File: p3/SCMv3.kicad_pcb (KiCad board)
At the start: 2 copper layers, 58.7 x 110.9 mm, 121 parts, among them IC1 40106, IC2 40106, IC3 TL082, J1 ISP, J1-OUT8 JACK-MONO-SWB, J2 Conn_01x02, J2-OUT7 JACK-MONO-SWB, J3 POWER, J3-OUT6 JACK-MONO-SWB, J4-OUT5 JACK-MONO-SWB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

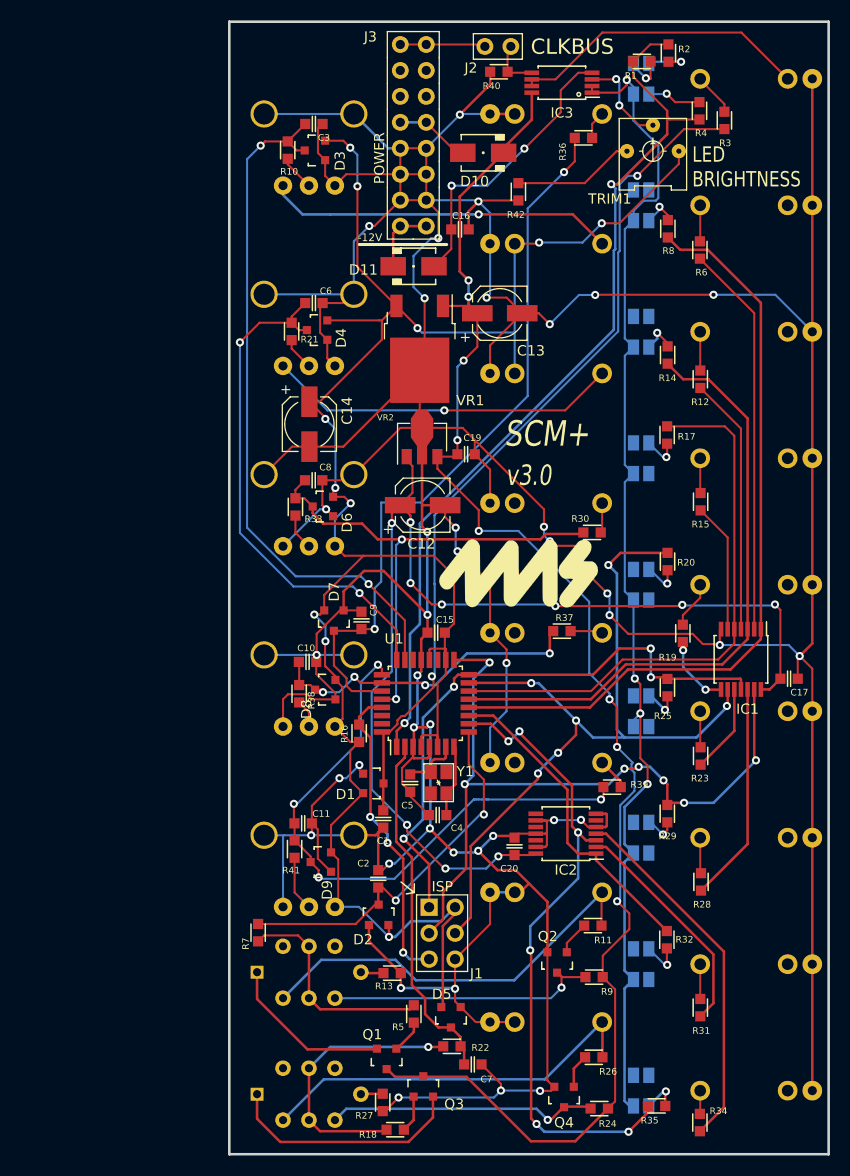
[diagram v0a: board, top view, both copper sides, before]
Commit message: p3 ready to connect pins: then route
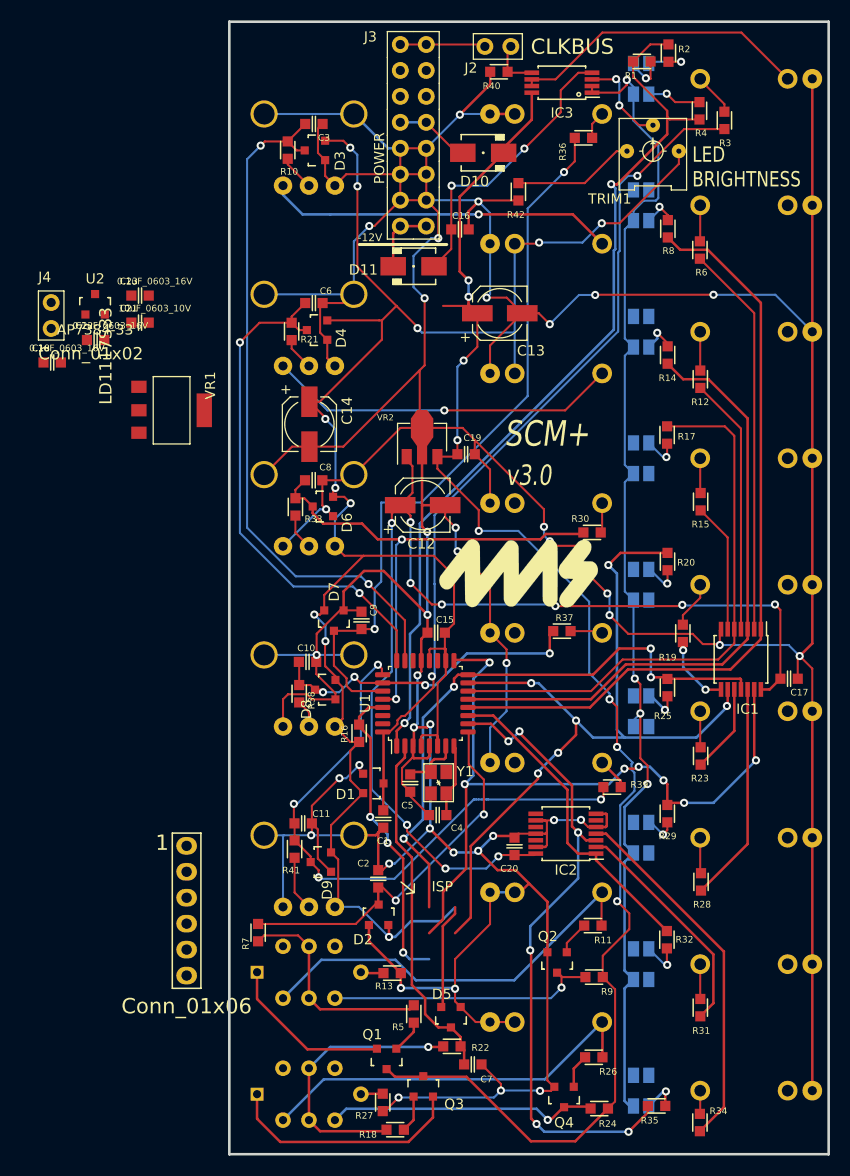
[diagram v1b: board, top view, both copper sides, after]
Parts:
- added C18: 0.1uF_0603_16V, 4ms_Capacitor:C_0603, F.Cu at (-17.3, 33.4)
- added C21: 10uF_0603_10V, 4ms_Capacitor:C_0603, F.Cu at (-8.74, 29.5)
- added C22: 0.1uF_0603_16V, 4ms_Capacitor:C_0603, F.Cu at (-13.1, 31.2)
- added C23: 0.1uF_0603_16V, 4ms_Capacitor:C_0603, F.Cu at (-8.74, 26.8)
- added J4: Conn_01x02, 4ms_Connector:Pins_1x02_2.54mm_TH, F.Cu at (-17.4, 28.8)
- added U2: AP7384-33, 4ms_Package_SOT:SOT23-3_PO132, F.Cu at (-13.1, 27.7)
- J1: value ISP -> Conn_01x06; footprint 4ms_Connector:Pins_2x03_2.54mm_TH -> 4ms_Connector:Pins_1x06_2.54mm_TH_SWD
- U1: value ATMEGA328-AU -> STM32F030K6Tx; footprint 4ms_Package_QFP:TQFP-32_7x7mm_P0.8mm -> Package_QFP:LQFP-32_7x7mm_P0.8mm
- VR1: value L78M05CDT -> LD1117S33; footprint 4ms_Package_TO:TO-252-2 -> 4ms_Package_SOT:SOT223
- moved J1 25.1 mm to (-4.18, 87.0)
- moved VR1 25.0 mm to (-5.65, 38.0)
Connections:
- net +9V renamed +8V
- net Net-(J2-Pad2) renamed /CLKBUS_PWRHDR
- C14 pad 1: +5V -> +3V3
- C15 pad 1: +5V -> -12VA
- IC1 pad 11: /UC_OUT5_MISO -> /UC_OUT5
- IC1 pad 13: /UC_OUT6_SCK -> /UC_OUT6
- IC1 pad 9: /UC_OUT4_MOSI -> /UC_OUT4
- J1 pad 1: /UC_OUT5_MISO -> +3V3
- J1 pad 2: +5V -> unconnected-(J1-Pad2)
- J1 pad 3: /UC_OUT6_SCK -> GND
- J1 pad 4: /UC_OUT4_MOSI -> /SWDIO
- J1 pad 6: GND -> unconnected-(J1-Pad6)
- R16 pad 2: +5V -> +3V3
- R20 pad 1: /UC_OUT4_MOSI -> /UC_OUT4
- R25 pad 1: /UC_OUT5_MISO -> /UC_OUT5
- R29 pad 1: /UC_OUT6_SCK -> /UC_OUT6
- TRIM1 pad 3: +5V -> +3V3
- U1 pad 1: /UC_LED_IN -> +3V3
- U1 pad 10: /UC_OUT8 -> unconnected-(U1-Pad10)
- U1 pad 11: /UC_OUT7 -> unconnected-(U1-Pad11)
- U1 pad 12: /UC_OUT1 -> unconnected-(U1-Pad12)
- U1 pad 13: /UC_OUT2 -> unconnected-(U1-Pad13)
- U1 pad 14: /UC_OUT3 -> unconnected-(U1-Pad14)
- U1 pad 15: /UC_OUT4_MOSI -> unconnected-(U1-Pad15)
- U1 pad 16: /UC_OUT5_MISO -> GND
- U1 pad 17: /UC_OUT6_SCK -> +3V3
- U1 pad 18: +5V -> unconnected-(U1-Pad18)
- U1 pad 2: /UC_MUTE -> Net-(C5-Pad1)
- U1 pad 20: +5V -> unconnected-(U1-Pad20)
- U1 pad 21: GND -> unconnected-(U1-Pad21)
- U1 pad 23: /UC_ROTATE -> /SWDIO
- U1 pad 24: /UC_SLIP -> /SWCLK
- U1 pad 25: /UC_PW -> unconnected-(U1-Pad25)
- U1 pad 26: /UC_SKIP -> unconnected-(U1-Pad26)
- U1 pad 27: /UC_SYNC -> unconnected-(U1-Pad27)
- U1 pad 28: /UC_SHUFFLE -> unconnected-(U1-Pad28)
- U1 pad 29: /RESET -> unconnected-(U1-Pad29)
- U1 pad 3: GND -> Net-(C4-Pad1)
- U1 pad 32: /UC_CLK_IN -> GND
- U1 pad 4: +5V -> /RESET
- U1 pad 5: GND -> +3.3VA
- U1 pad 6: +5V -> unconnected-(U1-Pad6)
- U1 pad 7: Net-(C5-Pad1) -> unconnected-(U1-Pad7)
- U1 pad 8: Net-(C4-Pad1) -> unconnected-(U1-Pad8)
- U1 pad 9: /UC_FAST -> unconnected-(U1-Pad9)
- VR1 pad 1: +12V -> GND
- VR1 pad 2: GND -> +3V3
- VR1 pad 3: +5V -> +12V
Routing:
- net GND: track 666.9 -> 938.0 mm, vias 40 -> 58
- net +5V: track 208.0 -> 10.3 mm, vias 11 -> 0
- net /UC_OUT4_MOSI: track 80.1 -> 0.00 mm, vias 6 -> 0
- net /UC_OUT4: track 0.00 -> 80.1 mm, vias 0 -> 6
- net /UC_OUT6_SCK: track 73.4 -> 0.00 mm, vias 7 -> 0
- net /UC_OUT5_MISO: track 58.7 -> 0.00 mm, vias 4 -> 0
- net /UC_OUT5: track 0.00 -> 58.7 mm, vias 0 -> 4
- net unconnected-(U1-Pad29): track 0.00 -> 30.3 mm, vias 0 -> 3
- net /RESET: track 30.3 -> 0.00 mm, vias 3 -> 0

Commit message: Atmega replacement and other mods
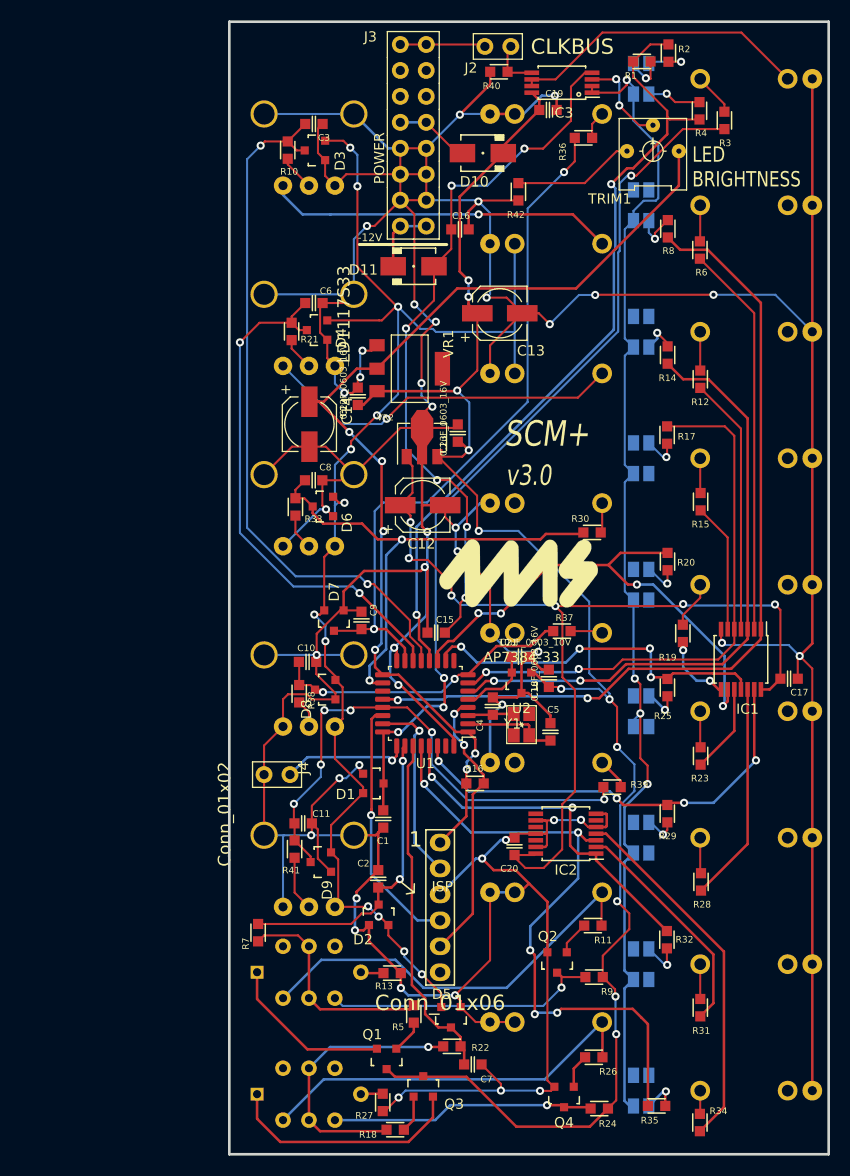
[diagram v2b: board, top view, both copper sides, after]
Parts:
- moved C18 57.6 mm to (31.3, 64.3), turned to 90 degrees
- moved U2 55.8 mm to (28.6, 64.7), turned to 180 degrees
- moved J4 50.1 mm to (4.67, 73.7), turned to -90 degrees
- moved C21 49.5 mm to (28.5, 62.2)
- moved C19 34.6 mm to (31.2, 8.64)
- moved C23 33.9 mm to (22.4, 40.3), turned to 90 degrees
- moved C22 26.3 mm to (12.6, 36.7), turned to 90 degrees
- moved J1 24.8 mm to (20.6, 86.7)
- moved VR1 23.7 mm to (17.7, 34.0)
- moved C5 14.6 mm to (31.4, 69.5), turned to 90 degrees
- moved R16 12.4 mm to (24.1, 74.6), turned to 180 degrees
- moved C4 12.0 mm to (25.8, 67.0), turned to 90 degrees
- moved Y1 9.91 mm to (28.6, 68.8), turned to -90 degrees
- turned U1 to 180 degrees
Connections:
- J1 pad 2: unconnected-(J1-Pad2) -> /SWCLK
- U1 pad 10: unconnected-(U1-Pad10) -> /UC_OUT5
- U1 pad 11: unconnected-(U1-Pad11) -> /UC_OUT4
- U1 pad 12: unconnected-(U1-Pad12) -> /UC_LED_IN
- U1 pad 13: unconnected-(U1-Pad13) -> /UC_ROTATE
- U1 pad 14: unconnected-(U1-Pad14) -> /UC_SLIP
- U1 pad 15: unconnected-(U1-Pad15) -> /UC_SYNC
- U1 pad 18: unconnected-(U1-Pad18) -> /UC_SHUFFLE
- U1 pad 20: unconnected-(U1-Pad20) -> /UC_OUT1
- U1 pad 21: unconnected-(U1-Pad21) -> /UC_PW
- U1 pad 22: unconnected-(U1-Pad22) -> /SWDIO
- U1 pad 23: /SWDIO -> /SWCLK
- U1 pad 24: /SWCLK -> /UC_CLK_IN
- U1 pad 25: unconnected-(U1-Pad25) -> /FREERUN_JMP
- U1 pad 26: unconnected-(U1-Pad26) -> /UC_FAST
- U1 pad 27: unconnected-(U1-Pad27) -> /UC_MUTE
- U1 pad 28: unconnected-(U1-Pad28) -> /UC_OUT8
- U1 pad 29: unconnected-(U1-Pad29) -> /UC_OUT7
- U1 pad 30: unconnected-(U1-Pad30) -> /UC_OUT6
- U1 pad 6: unconnected-(U1-Pad6) -> /UC_OUT2
- U1 pad 7: unconnected-(U1-Pad7) -> /UC_OUT3
- U1 pad 8: unconnected-(U1-Pad8) -> /UC_SKIP
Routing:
- net GND: track 938.0 -> 646.4 mm, vias 58 -> 41
- net +5V: track 10.3 -> 138.2 mm, vias 0 -> 12
- net +3V3: track 0.00 -> 102.7 mm, vias 0 -> 6
- net /UC_OUT6: track 0.00 -> 43.2 mm, vias 0 -> 4
- net -12VA: track 28.2 -> 70.0 mm, vias 2 -> 6
- net /UC_OUT4: track 80.1 -> 49.4 mm, vias 6 -> 4
- net unconnected-(U1-Pad29): track 30.3 -> 0.00 mm, vias 3 -> 0
- net /RESET: track 0.00 -> 27.3 mm, vias 0 -> 2
- net /SWDIO: track 0.00 -> 25.1 mm, vias 0 -> 1
- net /UC_OUT5: track 58.7 -> 35.5 mm
- net +12V: track 148.7 -> 168.0 mm, vias 8 -> 11
- net /SWCLK: track 0.00 -> 18.6 mm, vias 0 -> 1
- net +8V: track 109.3 -> 93.0 mm, vias 10 -> 6
- net /FREERUN_JMP: track 0.00 -> 12.4 mm, vias 0 -> 1
- net /UC_LED_IN: track 87.5 -> 78.8 mm
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
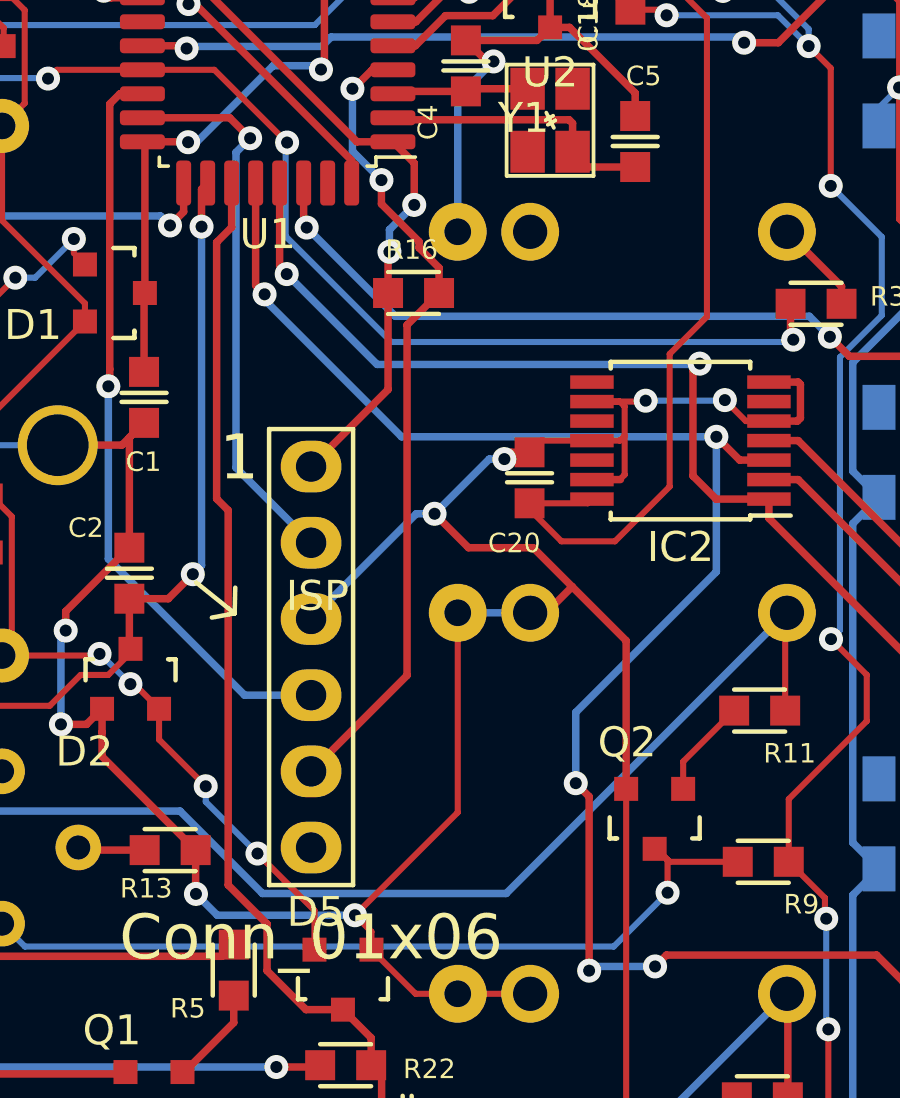
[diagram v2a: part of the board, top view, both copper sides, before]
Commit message: Notes on schematic about wrong pin assignments. Cleaned up schematic, too
To Do:
Sch: Some nets requiring an ADC pin are connected to non-ADC pins.
PCB:  Fix routing to pots with V+/GND swapped on pins 1/3. Also fix routing to ADC pins

Done:
Removed R16 (RESET->V+) and replaced with C24 (RESET->GND).
Connected BOOT0 to GND.
Flipped V+/GND on three pots that were backwards on last proto (fixed on schematic only)
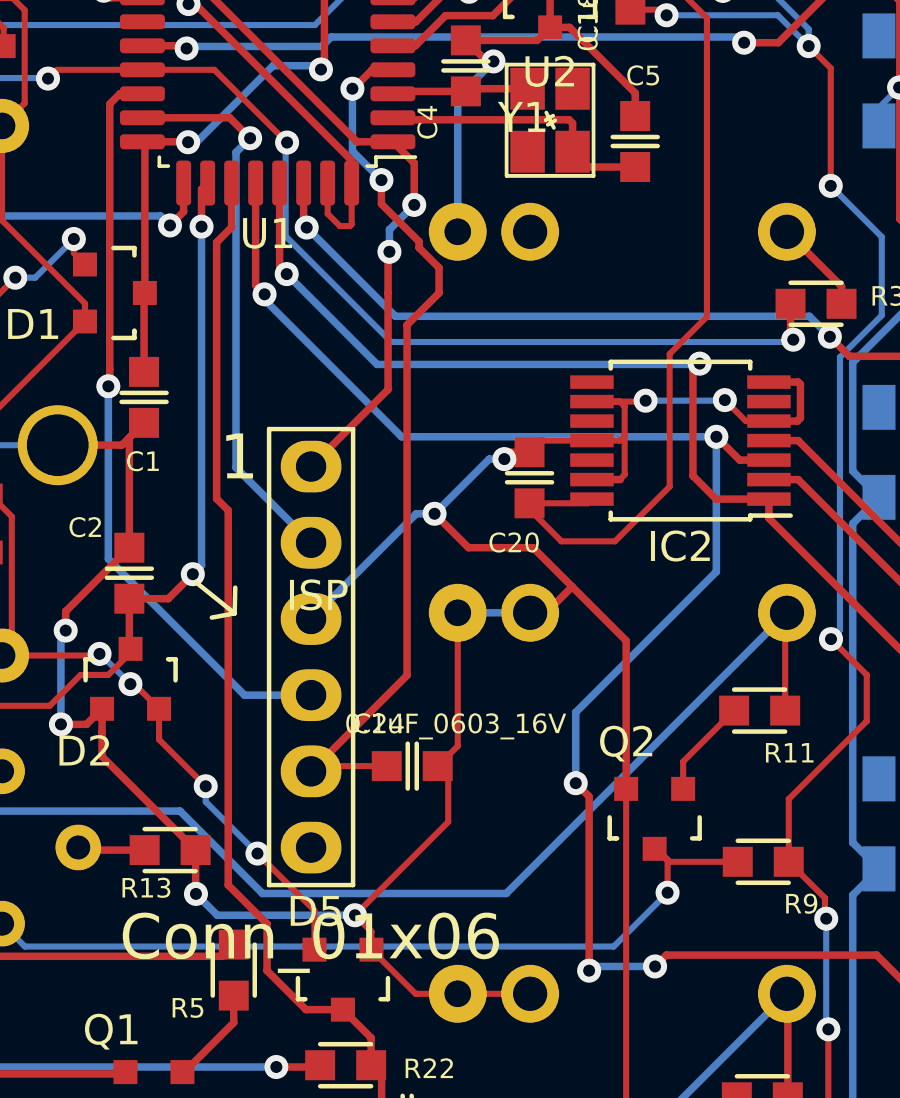
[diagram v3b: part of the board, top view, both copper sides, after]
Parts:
- removed R16: 10k_0603, 4ms_Resistor:R_0603
- added C24: 0.1uF_0603_16V, 4ms_Capacitor:C_0603, F.Cu at (24.0, 90.3)
- renumbered G*** to LOGO1
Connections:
- PPW1 pad 1: +5V -> GND
- PPW1 pad 3: GND -> +5V
- PSHUFFLE1 pad 1: +5V -> GND
- PSHUFFLE1 pad 3: GND -> +5V
- PSKIP1 pad 1: +5V -> GND
- PSKIP1 pad 3: GND -> +5V
- U1 pad 31: unconnected-(U1-Pad31) -> GND
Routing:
- net GND: track 646.4 -> 650.0 mm
- net /RESET: track 27.3 -> 29.9 mm

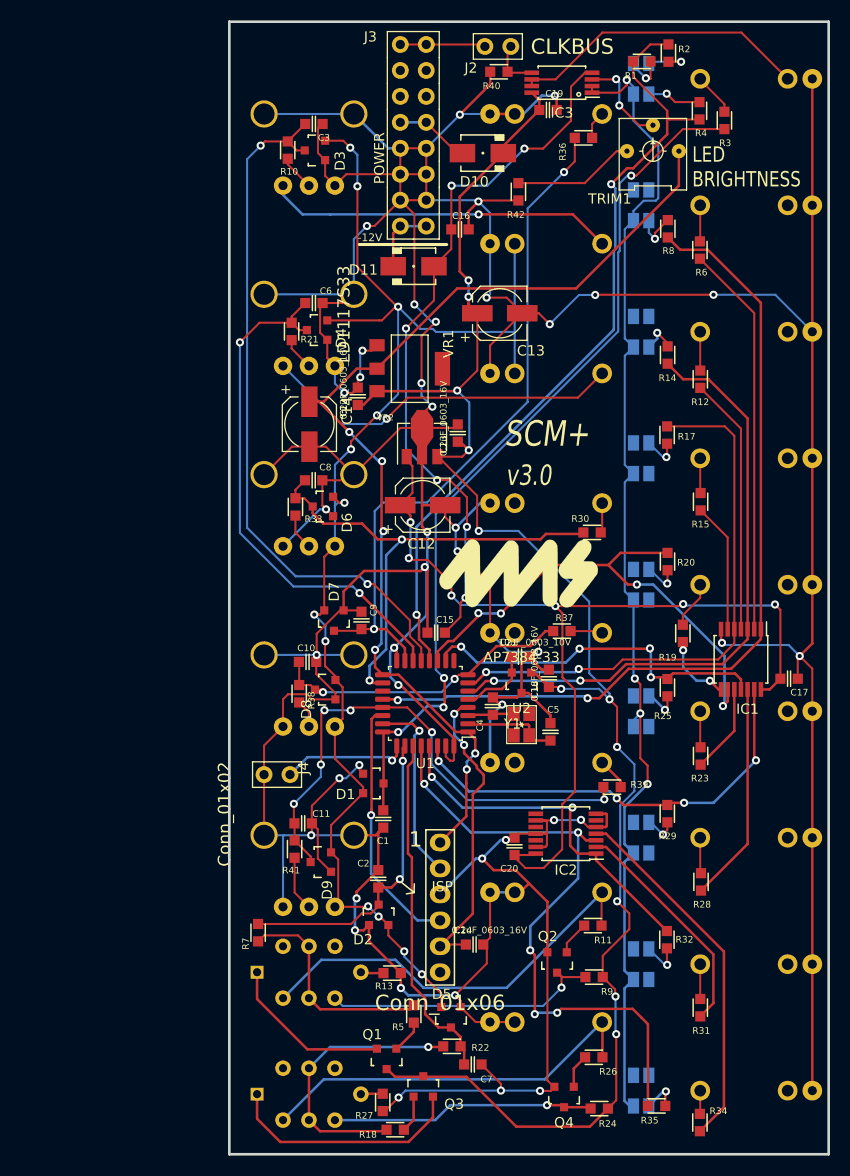
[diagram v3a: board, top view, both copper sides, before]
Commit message: Fixed errors in pcb and updated schematic accordingly
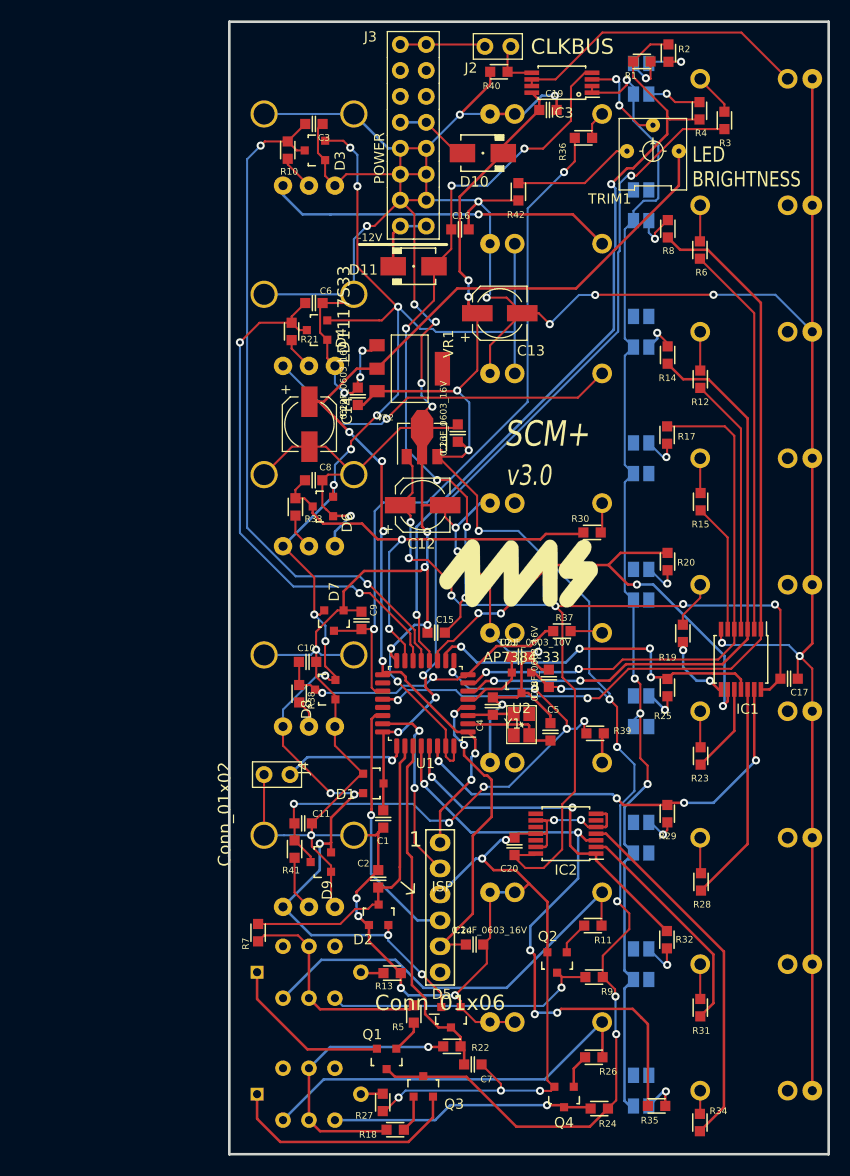
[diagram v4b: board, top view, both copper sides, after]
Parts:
- moved R39 5.52 mm to (35.8, 69.7)
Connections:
- U1 pad 15: /UC_SYNC -> /UC_SHUFFLE
- U1 pad 18: /UC_SHUFFLE -> unconnected-(U1-Pad18)
- U1 pad 19: unconnected-(U1-Pad19) -> /UC_SYNC
- U1 pad 21: /UC_PW -> unconnected-(U1-Pad21)
- U1 pad 9: unconnected-(U1-Pad9) -> /UC_PW
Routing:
- net +5V: track 138.2 -> 155.7 mm, vias 12 -> 14
- net GND: track 650.0 -> 633.2 mm, vias 41 -> 40
- net /UC_PW: track 51.2 -> 56.2 mm, vias 6 -> 7
- net /UC_SHUFFLE: track 49.2 -> 45.7 mm
- net /UC_SYNC: track 67.8 -> 69.8 mm
- net /RESET: track 29.9 -> 30.7 mm
- net /UC_CLK_IN: track 86.4 -> 85.6 mm
- net /UC_SLIP: track 51.7 -> 52.3 mm
- net /UC_OUT1: track 84.4 -> 84.9 mm
- net /UC_FAST: vias 2 -> 0
- net /SWCLK: vias 1 -> 2

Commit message: Fixed errors on pcb and schem
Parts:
- PPW1, PROTATE1, PSHUFFLE1, PSKIP1, PSLIP1: value 9mm_CtrDet_10k_DShaft -> 9mm_NoDet_100k_Knurled_Lined; footprint 4ms_Potentiometer:Pot_9mm_Dshaft_Det -> 4ms_Potentiometer:Pot_9mm_Knurl_NoDet
- R4: value 4.7k_0603 -> 10k_0603
